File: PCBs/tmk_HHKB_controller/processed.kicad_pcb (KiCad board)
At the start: 2 copper layers, 141.5 x 36 mm, 95 parts, among them CN1 JP, CN2 PRO2, J1 USB_mini_micro_B, P1 GND, P10 CONN_1, P100 LIPO, P11 CONN_1, P110 CONN_1, P111 CONN_1, P112 CONN_1, P113 CONN_1, P114 CONN_1, P115 CONN_1, P12 CONN_1, P13 CONN_1, P14 CONN_1, P15 CONN_1, P2 D+, P3 D-, P4 VUSB, P5 PD1, P6 PD0, P7 GND, P8 CONN_3X2, P9 CONN_1, Q1 Nch, Q10 Nch, Q2 Nch, Q3 Nch, Q4 Pch, Q5 Pch, SW1 SW_PUSH, SW2 SW_DPDT, U1 ATMEGA32U4, U2 MIC5504-3.3YMTR, U3 NCP1402SN50, U4 MCP73832, U5 RN42, X1 16MHz

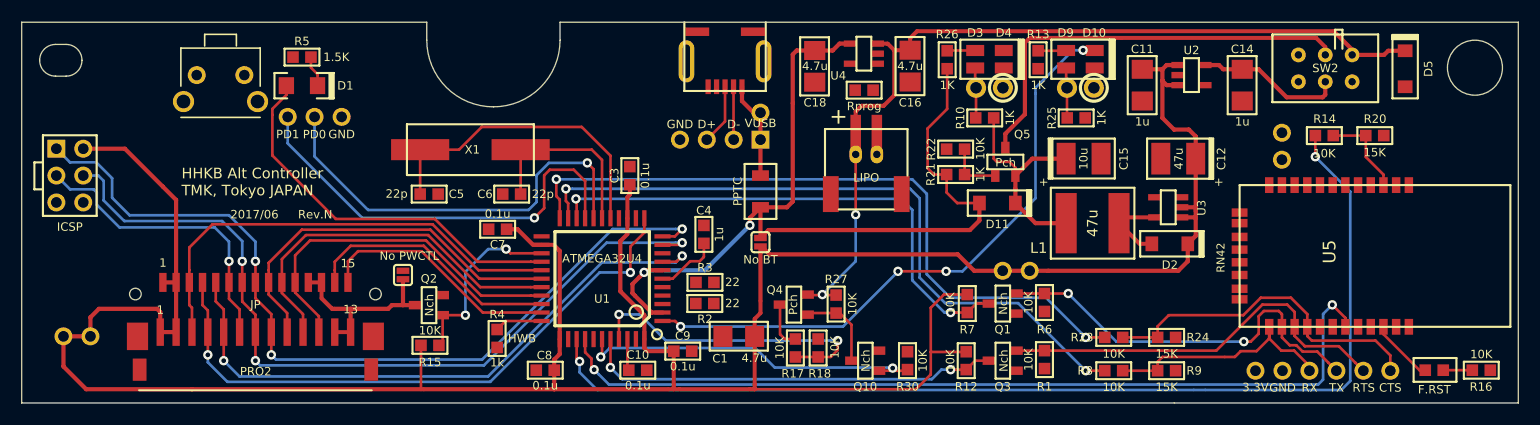
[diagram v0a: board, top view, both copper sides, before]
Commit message: recheck all circuits and clean up fill zone by rerouting the nets using freerouting and manually
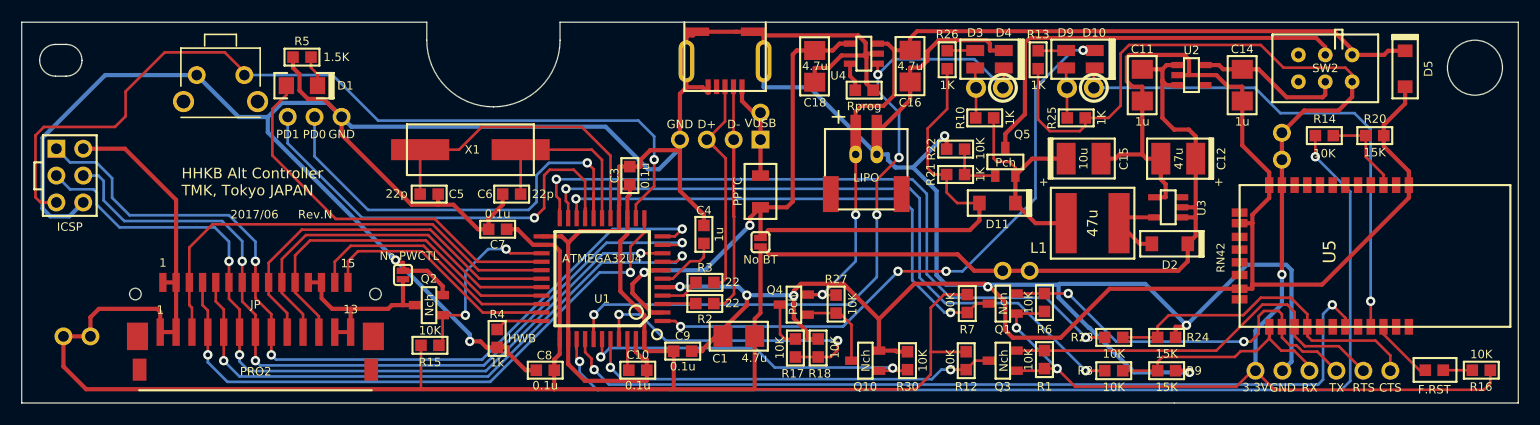
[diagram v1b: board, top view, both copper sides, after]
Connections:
- C1 pad 2: (no net) -> GND
- C10 pad 2: (no net) -> GND
- C11 pad 2: (no net) -> GND
- C12 pad 2: (no net) -> GND
- C14 pad 2: (no net) -> GND
- C15 pad 2: (no net) -> GND
- C16 pad 2: (no net) -> GND
- C18 pad 2: (no net) -> GND
- C3 pad 2: (no net) -> GND
- C4 pad 2: (no net) -> GND
- C5 pad 2: (no net) -> GND
- C6 pad 2: (no net) -> GND
- C7 pad 2: (no net) -> GND
- C8 pad 2: (no net) -> GND
- C9 pad 2: (no net) -> GND
- D10 pad 2: (no net) -> /bluetooth/LED_STS
- D3 pad 2: (no net) -> ~CHRG
- D3 pad 4: (no net) -> GND
- D4 pad 2: (no net) -> ~CHRG
- D5 pad 1: (no net) -> GND
- D9 pad 2: (no net) -> /bluetooth/LED_STS
- J1 pad 4: (no net) -> Net-(J1-Pad4)
- J1 pad 5: (no net) -> GND
- J1 pad 6: (no net) -> GND
- JP3 pad 1: (no net) -> GND
- P1 pad 1: (no net) -> GND
- P100 pad 2: (no net) -> GND
- P110 pad 1: (no net) -> +3.3V
- P113 pad 1: (no net) -> GND
- P13 pad 1: (no net) -> +3.3V
- P15 pad 1: (no net) -> +3.3V
- P7 pad 1: (no net) -> GND
- P8 pad 5: (no net) -> /~RESET
- P8 pad 6: (no net) -> GND
- Q1 pad G: (no net) -> +3.3V
- Q10 pad S: (no net) -> GND
- Q2 pad S: (no net) -> GND
- Q3 pad G: (no net) -> +3.3V
- R1 pad 1: (no net) -> +3.3V
- R11 pad 1: (no net) -> Net-(R11-Pad1)
- R11 pad 2: (no net) -> GND
- R13 pad 2: (no net) -> +3.3V
- R16 pad 1: (no net) -> +3.3V
- R18 pad 2: (no net) -> GND
- R2 pad 1: (no net) -> Net-(R2-Pad1)
- R2 pad 2: (no net) -> /D-
- R20 pad 2: (no net) -> GND
- R22 pad 2: (no net) -> GND
- R24 pad 2: (no net) -> GND
- R25 pad 1: (no net) -> +3.3V
- R3 pad 1: (no net) -> Net-(R3-Pad1)
- R3 pad 2: (no net) -> /D+
- R30 pad 2: (no net) -> GND
- R4 pad 1: (no net) -> GND
- R5 pad 2: (no net) -> GND
- R6 pad 1: (no net) -> +3.3V
- R9 pad 2: (no net) -> GND
- SW1 pad 1: (no net) -> GND
- SW1 pad 2: (no net) -> /~RESET
- SW2 pad 3: (no net) -> Net-(SW2-Pad3)
- SW2 pad 5: (no net) -> +3.3V
- SW2 pad 6: (no net) -> Net-(SW2-Pad6)
- U1 pad 13: (no net) -> /~RESET
- U1 pad 15: (no net) -> GND
- U1 pad 23: (no net) -> GND
- U1 pad 35: (no net) -> GND
- U1 pad 38: (no net) -> ~CHRG
- U1 pad 43: (no net) -> GND
- U1 pad 5: (no net) -> GND
- U1 pad 9: (no net) -> /PB1
- U2 pad 2: (no net) -> GND
- U2 pad 4: (no net) -> Net-(U2-Pad4)
- U3 pad 3: (no net) -> Net-(U3-Pad3)
- U3 pad 4: (no net) -> GND
- U4 pad 1: (no net) -> ~CHRG
- U4 pad 2: (no net) -> GND
- U4 pad 5: (no net) -> Net-(R11-Pad1)
- U5 pad 1: (no net) -> GND
- U5 pad 10: (no net) -> Net-(U5-Pad10)
- U5 pad 11: (no net) -> +3.3V
- U5 pad 12: (no net) -> GND
- U5 pad 17: (no net) -> Net-(U5-Pad17)
- U5 pad 18: (no net) -> Net-(U5-Pad18)
- U5 pad 2: (no net) -> /bluetooth/SPI_MOSI
- U5 pad 20: (no net) -> Net-(U5-Pad20)
- U5 pad 21: (no net) -> /bluetooth/LED_STS
- U5 pad 23: (no net) -> /bluetooth/SPI_SS
- U5 pad 24: (no net) -> /bluetooth/SPI_MISO
- U5 pad 28: (no net) -> GND
- U5 pad 29: (no net) -> GND
- U5 pad 30: (no net) -> Net-(U5-Pad30)
- U5 pad 31: (no net) -> /bluetooth/LED_ACT
- U5 pad 32: (no net) -> Net-(U5-Pad32)
- U5 pad 33: (no net) -> Net-(U5-Pad33)
- U5 pad 34: (no net) -> Net-(U5-Pad34)
- U5 pad 35: (no net) -> Net-(U5-Pad35)
- U5 pad 4: (no net) -> Net-(U5-Pad4)
- U5 pad 5: (no net) -> /bluetooth/RN42_RST
- U5 pad 6: (no net) -> /bluetooth/SPI_SCK
- U5 pad 7: (no net) -> Net-(U5-Pad7)
- U5 pad 8: (no net) -> Net-(U5-Pad8)
- U5 pad 9: (no net) -> Net-(U5-Pad9)
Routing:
- net GND: track 0.00 -> 555.1 mm, vias 0 -> 9
- net +3.3V: track 0.00 -> 134.8 mm, vias 0 -> 3
- net /~RESET: track 0.00 -> 83.7 mm, vias 0 -> 1
- net ~CHRG: track 0.00 -> 69.0 mm, vias 0 -> 4
- net /bluetooth/LED_STS: track 0.00 -> 48.4 mm, vias 0 -> 1
- net /PB1: track 28.5 -> 76.3 mm, vias 1 -> 3
- net /D-: track 5.01 -> 29.3 mm
- net /D+: track 5.72 -> 22.0 mm
- net Net-(R3-Pad1): track 0.00 -> 3.83 mm
- net Net-(R2-Pad1): track 0.00 -> 3.26 mm
- net Net-(C5-Pad1): track 30.1 -> 33.1 mm
- net Net-(R11-Pad1): track 0.00 -> 2.70 mm
- net /PD0: track 40.4 -> 42.7 mm
- net /AREF: track 2.99 -> 4.39 mm
- net ADC_LIPO: track 29.2 -> 30.4 mm
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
